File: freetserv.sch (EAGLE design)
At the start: 157 parts, among them IC1 MCP16311-E/MS, IC10 MAX3232ECPW, IC11 MAX3232ECPW, IC12 MAX3232ECPW, IC13 MAX3232ECPW, IC14 FT4232HL, IC15 MAX3232ECPW, IC16 MAX3232ECPW, IC17 MAX3232ECPW, IC18 MAX3232ECPW, IC3 TUSB2046BVF, IC4 FT4232HL, IC5 MAX3232ECPW, IC6 MAX3232ECPW, IC7 MAX3232ECPW, IC8 MAX3232ECPW, IC9 FT4232HL, Q2 6MHz

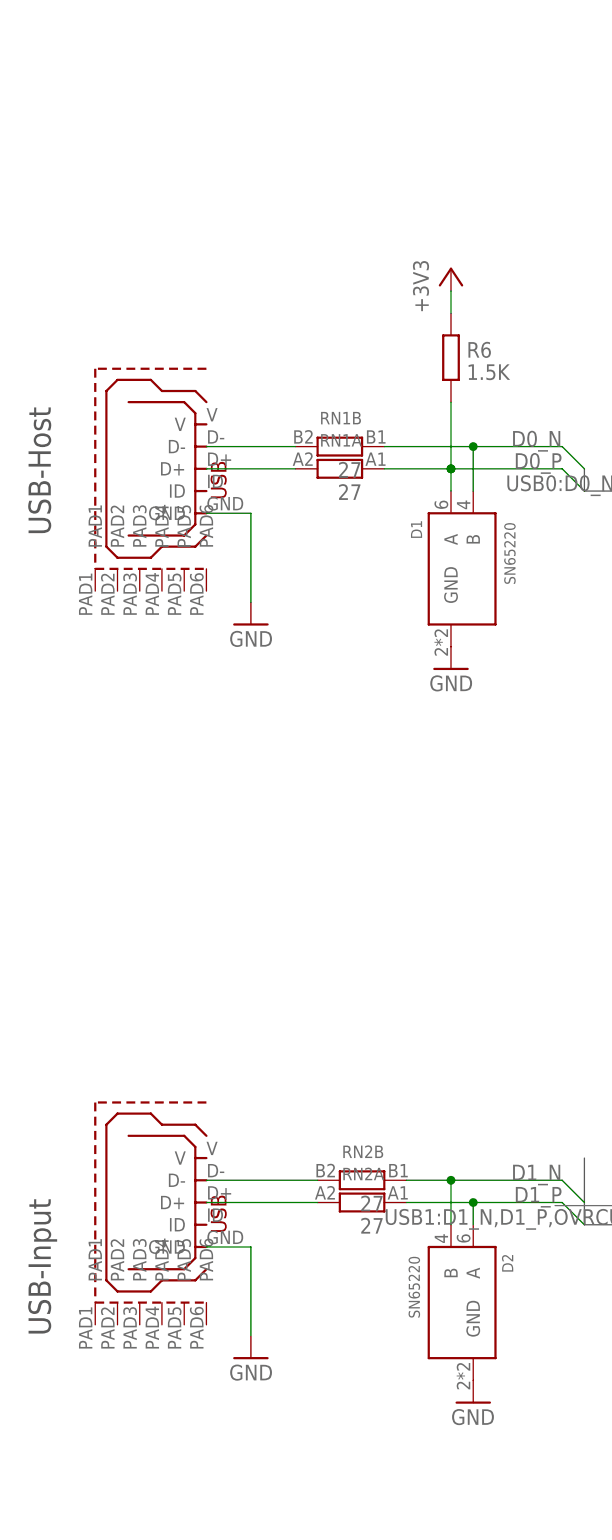
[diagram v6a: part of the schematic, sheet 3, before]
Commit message: add daisy-chain input/output socket/pin headers
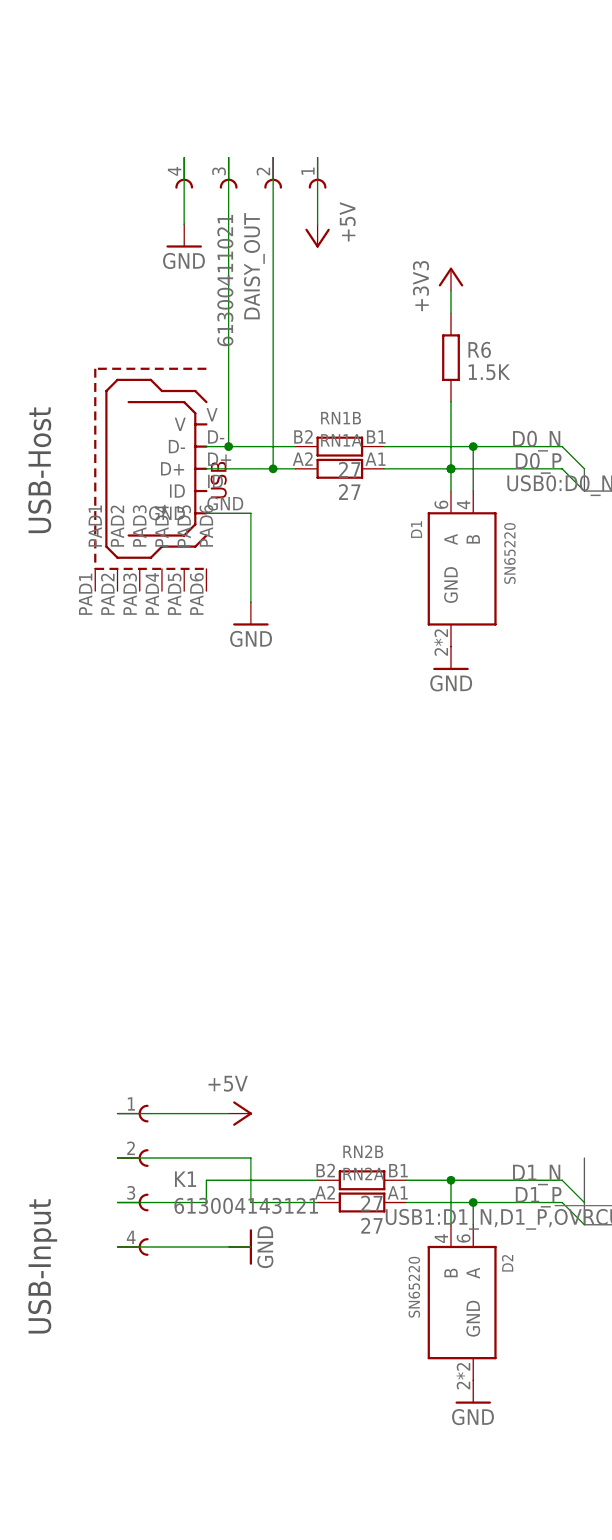
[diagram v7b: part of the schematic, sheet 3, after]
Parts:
- removed USB_OUT: USB_MICROB, ftdi_ft231xq-r:USB_MICROB
- added DAISY_OUT: 61300411021, Wurth_Elektronik_Electromechanic_Board_to_Board_Connectors_rev15c:61300411021
- added K1: 613004143121, Wurth_Elektronik_Electromechanic_Board_to_Board_Connectors_rev15c:613004143121
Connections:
- removed net DX1_P: RN2A.2, USB_OUT.D+
- new net N$15: K1.4
- new net N$8: K1.3, RN2B.2
- net +5V: now also DAISY_OUT.1, K1.1
- net DX0_N: now also DAISY_OUT.3
- net DX0_P: now also DAISY_OUT.2
- net GND: now also DAISY_OUT.4; no longer USB_OUT.GND
- net N$7: now also K1.2, RN2A.2; no longer RN2B.2, USB_OUT.D-
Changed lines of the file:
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@@
 </part>
 <part name="GND11" library="supply1" deviceset="GND" device=""/>
-<part name="USB_OUT" library="ftdi_ft231xq-r" deviceset="USB_MICROB" device="">
-<attribute name="PARTNO" value="H11634CT-ND"/>
-</part>
-<part name="GND37" library="supply1" deviceset="GND" device=""/>
 <part name="C36" library="resistor" deviceset="C-EU" device="C0805" value="0.1uF">
 <attribute name="PARTNO" value="1276-1003-1-ND"/>
@@
 <part name="P+1" library="supply1" deviceset="+5V" device=""/>
 <part name="GND2" library="supply1" deviceset="GND" device=""/>
+<part name="DAISY_OUT" library="Wurth_Elektronik_Electromechanic_Board_to_Board_Connectors_rev15c" deviceset="61300411021" device=""/>
+<part name="P+14" library="supply1" deviceset="+5V" device=""/>
+<part name="GND8" library="supply1" deviceset="GND" device=""/>
+<part name="P+15" library="supply1" deviceset="+5V" device=""/>
+<part name="GND17" library="supply1" deviceset="GND" device=""/>
+<part name="K1" library="Wurth_Elektronik_Electromechanic_Board_to_Board_Connectors_rev15c" deviceset="613004143121" device=""/>
 </parts>
 <sheets>
@@
 </plain>
 <instances>
+<instance part="K1" gate="G$1" x="33.02" y="45.72"/>
 <instance part="PWRIN" gate="G$1" x="25.4" y="231.14"/>
 <instance part="P+1" gate="1" x="38.1" y="233.68" rot="R270"/>
@@
 <attribute name="PARTNO" x="213.36" y="215.9" size="1.778" layer="96" display="off"/>
 </instance>
-<instance part="USB_OUT" gate="G$1" x="35.56" y="41.91">
-<attribute name="PARTNO" x="35.56" y="41.91" size="1.778" layer="96" rot="R270" display="off"/>
-</instance>
-<instance part="GND37" gate="1" x="40.64" y="25.4" rot="MR0"/>
 <instance part="C36" gate="G$1" x="175.26" y="165.1">
 <attribute name="PARTNO" x="175.26" y="165.1" size="1.778" layer="96" display="off"/>
@@
 <instance part="P+10" gate="G$1" x="238.76" y="129.54" rot="MR90"/>
 <instance part="P+13" gate="G$1" x="238.76" y="147.32" rot="MR90"/>
+<instance part="DAISY_OUT" gate="G$1" x="40.64" y="154.94" rot="R270"/>
+<instance part="P+14" gate="1" x="48.26" y="152.4" rot="R180"/>
+<instance part="GND8" gate="1" x="33.02" y="152.4"/>
+<instance part="P+15" gate="1" x="40.64" y="53.34" rot="R270"/>
+<instance part="GND17" gate="1" x="40.64" y="38.1" rot="R90"/>
 </instances>
 <busses>
@@
 <pinref part="R5" gate="G$1" pin="2"/>
 <pinref part="GND4" gate="1" pin="GND"/>
-</segment>
-<segment>
-<pinref part="GND37" gate="1" pin="GND"/>
-<wire x1="40.64" y1="27.94" x2="40.64" y2="38.1" width="0.1524" layer="91"/>
-<wire x1="40.64" y1="38.1" x2="35.56" y2="38.1" width="0.1524" layer="91"/>
-<pinref part="USB_OUT" gate="G$1" pin="GND"/>
 </segment>
 <segment>
@@
 <pinref part="GND142" gate="1" pin="GND"/>
 <wire x1="274.32" y1="223.52" x2="274.32" y2="220.98" width="0.1524" layer="91"/>
+</segment>
+<segment>
+<pinref part="GND8" gate="1" pin="GND"/>
+<pinref part="DAISY_OUT" gate="G$1" pin="4"/>
+<wire x1="33.02" y1="154.94" x2="33.02" y2="162.56" width="0.1524" layer="91"/>
 </segment>
 </net>
@@
 <wire x1="129.54" y1="220.98" x2="129.54" y2="226.06" width="0.1524" layer="91"/>
 </segment>
+<segment>
+<pinref part="P+15" gate="1" pin="+5V"/>
+<pinref part="K1" gate="G$1" pin="1"/>
+<wire x1="38.1" y1="53.34" x2="25.4" y2="53.34" width="0.1524" layer="91"/>
+</segment>
+<segment>
+<pinref part="P+14" gate="1" pin="+5V"/>
+<pinref part="DAISY_OUT" gate="G$1" pin="1"/>
+<wire x1="48.26" y1="154.94" x2="48.26" y2="162.56" width="0.1524" layer="91"/>
+</segment>
 </net>
 <net name="N$3" class="0">
@@
 <segment>
 <pinref part="USB_HOST" gate="G$1" pin="D-"/>
-<wire x1="35.56" y1="129.54" x2="45.72" y2="129.54" width="0.1524" layer="91"/>
+<wire x1="35.56" y1="129.54" x2="38.1" y2="129.54" width="0.1524" layer="91"/>
 <pinref part="RN1" gate="B" pin="2"/>
+<pinref part="DAISY_OUT" gate="G$1" pin="3"/>
+<wire x1="38.1" y1="129.54" x2="45.72" y2="129.54" width="0.1524" layer="91"/>
+<wire x1="38.1" y1="129.54" x2="38.1" y2="162.56" width="0.1524" layer="91"/>
+<junction x="38.1" y="129.54"/>
 </segment>
 </net>
@@
 <pinref part="USB_HOST" gate="G$1" pin="D+"/>
 <pinref part="RN1" gate="A" pin="2"/>
-<wire x1="45.72" y1="127" x2="35.56" y2="127" width="0.1524" layer="91"/>
-</segment>
-</net>
-<net name="DX1_P" class="1">
-<segment>
-<pinref part="USB_OUT" gate="G$1" pin="D+"/>
-<pinref part="RN2" gate="A" pin="2"/>
-<wire x1="48.26" y1="43.18" x2="35.56" y2="43.18" width="0.1524" layer="91"/>
+<wire x1="45.72" y1="127" x2="43.18" y2="127" width="0.1524" layer="91"/>
+<pinref part="DAISY_OUT" gate="G$1" pin="2"/>
+<wire x1="43.18" y1="127" x2="35.56" y2="127" width="0.1524" layer="91"/>
+<wire x1="43.18" y1="127" x2="43.18" y2="162.56" width="0.1524" layer="91"/>
+<junction x="43.18" y="127"/>
 </segment>
 </net>
@@
 </segment>
 </net>
-<net name="N$7" class="1">
-<segment>
-<pinref part="USB_OUT" gate="G$1" pin="D-"/>
+<net name="N$7" class="0">
+<segment>
+<pinref part="RN2" gate="A" pin="2"/>
+<wire x1="48.26" y1="43.18" x2="40.64" y2="43.18" width="0.1524" layer="91"/>
+<wire x1="40.64" y1="43.18" x2="40.64" y2="48.26" width="0.1524" layer="91"/>
+<pinref part="K1" gate="G$1" pin="2"/>
+<wire x1="40.64" y1="48.26" x2="25.4" y2="48.26" width="0.1524" layer="91"/>
+</segment>
+</net>
+<net name="N$8" class="0">
+<segment>
 <pinref part="RN2" gate="B" pin="2"/>
 <wire x1="48.26" y1="45.72" x2="35.56" y2="45.72" width="0.1524" layer="91"/>
-</segment>
-</net>
+<wire x1="35.56" y1="45.72" x2="35.56" y2="43.18" width="0.1524" layer="91"/>
+<pinref part="K1" gate="G$1" pin="3"/>
+<wire x1="35.56" y1="43.18" x2="25.4" y2="43.18" width="0.1524" layer="91"/>
+</segment>
+</net>
+<net name="N$15" class="0">
+<segment>
+<pinref part="K1" gate="G$1" pin="4"/>
+<wire x1="40.64" y1="38.1" x2="25.4" y2="38.1" width="0.1524" layer="91"/>
+</segment>
+</net>

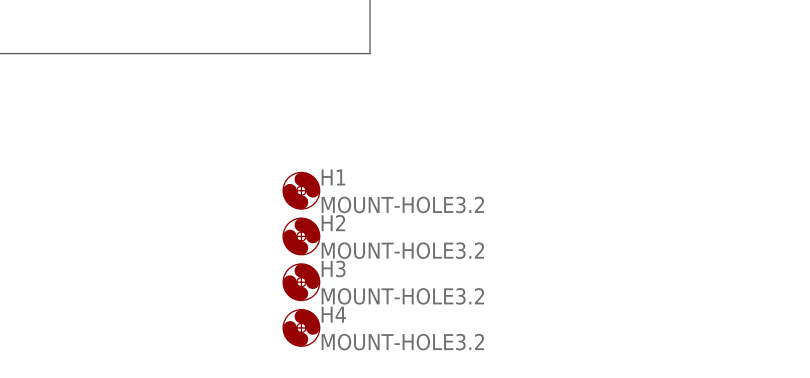
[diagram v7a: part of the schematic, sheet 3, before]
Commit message: drc: fix via size, width on bottom layer
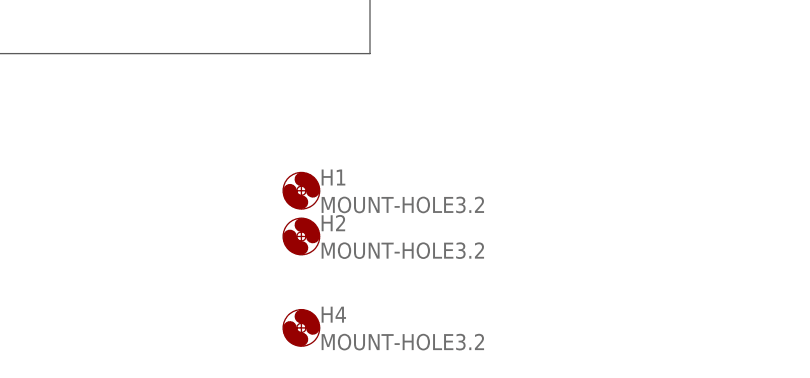
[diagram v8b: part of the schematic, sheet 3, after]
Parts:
- removed H3: MOUNT-HOLE3.2, holes:MOUNT-HOLE3.2
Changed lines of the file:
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@@
 <part name="H1" library="holes" deviceset="MOUNT-HOLE" device="3.2"/>
 <part name="H2" library="holes" deviceset="MOUNT-HOLE" device="3.2"/>
-<part name="H3" library="holes" deviceset="MOUNT-HOLE" device="3.2"/>
 <part name="H4" library="holes" deviceset="MOUNT-HOLE" device="3.2"/>
 <part name="RN1" library="resistor-net" deviceset="EXBV4V" device="" value="27"/>
@@
 <instance part="H1" gate="G$1" x="259.08" y="25.4"/>
 <instance part="H2" gate="G$1" x="259.08" y="20.32"/>
-<instance part="H3" gate="G$1" x="259.08" y="15.24"/>
 <instance part="H4" gate="G$1" x="259.08" y="10.16"/>
 <instance part="RN1" gate="B" x="50.8" y="129.54" rot="MR0"/>
